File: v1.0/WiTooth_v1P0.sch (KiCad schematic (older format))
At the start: 51 parts, among them P1 USB_A, P2 JTAG, P3 CONN_01X04, P4 CONN_01X20, P5 CONN_01X20, Q1 Q_NPN_EBC, Q2 Q_NPN_EBC, SW1 RESET, SW2 Switch_SPDT_x2, SW3 USER_SW, U1 AMS1117-3V3, U2 CP2102, U3 ESP-32_WROOM32_Rectangle, Y1 Crystal

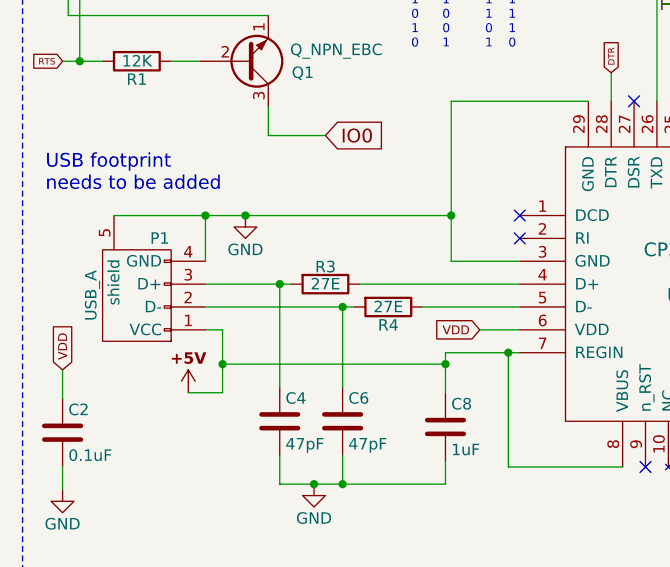
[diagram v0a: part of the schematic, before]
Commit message: schematic half verified; footprint association done
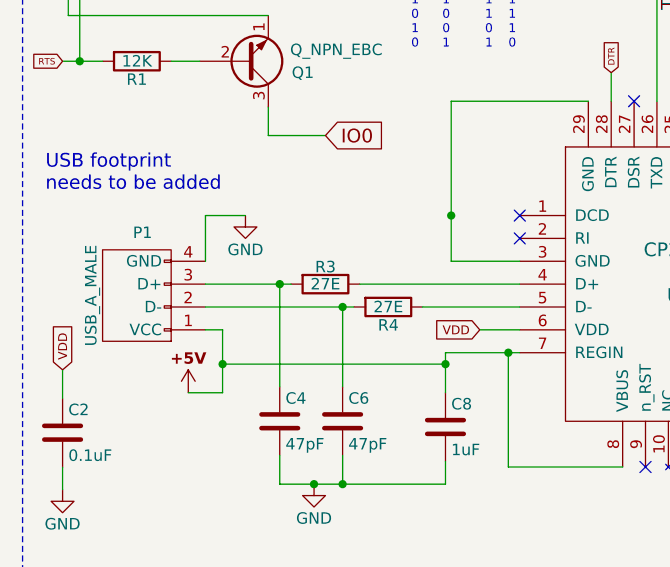
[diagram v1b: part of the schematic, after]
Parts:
- removed P1: USB_A, symbol USB_A
- added P1: USB_A_MALE, USB:usb-PCB_male, symbol USB_A_MALE
- U3: footprint (none) -> ESP-32:ESP32-WROOM
- Y1: footprint (none) -> Crystals:Crystal_AT310_d3.0mm_l10.0mm_Horizontal_1EP_style1
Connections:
- net +5V: now also P1.1 (VCC)
- net GND: now also P1.4 (GND); no longer U2.29 (GND), U2.3 (GND)
- net at C6.1, R4.2: now also P1.2 (D-)
- net at C4.1, R3.2: now also P1.3 (D+)
- new net: U2.29 (GND), U2.3 (GND)

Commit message: all changes done; schematic verified
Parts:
- removed C3: DNM, Capacitors_SMD:C_0805_HandSoldering, symbol C_Small
- removed C7: 22uF, Capacitors_SMD:C_0805_HandSoldering, symbol C
- removed R6: 5K, Resistors_SMD:R_0805_HandSoldering, symbol R
- C1: value 0.1uF -> 10uF
- C4: renamed from C5; value 47uF -> 10uF
- R11: renamed from R12; value 1K -> 470E
- R13: renamed from R14; value 10K -> 5K
- R7: renamed from R10; value 12K -> 470E
- renumbered C12 to C10, C13 to C11, C14 to C12, C15 to C13, C4 to C3, C6 to C5, C8 to C6, C9 to C7, C10 to C8, C11 to C9, R11 to R10, R13 to R12, R15 to R14, R16 to R15, R17 to R16, R5 to R4, R4 to R5, R7 to R6
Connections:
- net +3V3: now also R13.2; no longer R13.1
- net IO27: now also R7.2
- net IO32: no longer R7.2
- net at SW2.1 (A): now also R13.1; no longer R13.2
- net CTS: no longer names the net of U2.23 (CTS)
- no-connect marks 4 -> 5
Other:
- note removed: "check if switch\nis required\nor push button"
- moved on the sheet: C7, D1, D4, D5, R10, R11, R13, R4, R6, R7, SW2A

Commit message: initial placement started
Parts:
- U1: footprint TO_SOT_Packages_SMD:SOT-223-3Lead_TabPin2 -> TO_SOT_Packages_SMD:SOT-223
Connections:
- net GND: now also U3.39 (GND)
- no-connect marks 5 -> 7
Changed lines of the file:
@@
 F 0 "U1" H 1500 875 50  0000 C CNN
 F 1 "AMS1117-3V3" H 1400 1375 50  0000 C CNN
-F 2 "TO_SOT_Packages_SMD:SOT-223-3Lead_TabPin2" H 1400 1125 50  0001 C CNN
+F 2 "TO_SOT_Packages_SMD:SOT-223" H 1400 1125 50  0001 C CNN
 F 3 "" H 1500 875 50  0000 C CNN
 F 4 "LM1117 800-mA Low-Dropout Linear Regulator" H 1800 1175 61  0001 C CNN "DESC"
@@
 	1700 1125 2125 1125
 NoConn ~ 3600 3850
+NoConn ~ 3450 5450
+NoConn ~ 3550 5450
+Wire Wire Line
+	9075 3675 8825 3675
+Connection ~ 8825 3675
 $EndSCHEMATC

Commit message: basic placement done
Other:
- note removed: "Crystal footprint\nneeds to be added"
- note removed: "ESP32 footprint\nneeds to be added"
- note removed: "USB footprint\nneeds to be added"
- moved on the sheet: C2, P2, P3
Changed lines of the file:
@@
 L CONN_01X04 P3
 U 1 1 5898386C
-P 2925 6550
-F 0 "P3" H 2925 6800 50  0000 C CNN
-F 1 "CONN_01X04" V 3025 6550 50  0000 C CNN
-F 2 "Pin_Headers:Pin_Header_Straight_1x04_Pitch2.54mm" H 2925 6550 50  0001 C CNN
-F 3 "" H 2925 6550 50  0000 C CNN
-	1    2925 6550
+P 3550 6550
+F 0 "P3" H 3550 6800 50  0000 C CNN
+F 1 "CONN_01X04" V 3650 6550 50  0000 C CNN
+F 2 "Pin_Headers:Pin_Header_Straight_1x04_Pitch2.54mm" H 3550 6550 50  0001 C CNN
+F 3 "" H 3550 6550 50  0000 C CNN
+	1    3550 6550
 	-1   0    0    -1
 $EndComp
@@
 L +3V3 #PWR021
 U 1 1 58983CE6
-P 3350 6400
-F 0 "#PWR021" H 3350 6250 50  0001 C CNN
-F 1 "+3V3" H 3350 6550 50  0001 C CNN
-F 2 "" H 3350 6400 50  0000 C CNN
-F 3 "" H 3350 6400 50  0000 C CNN
-	1    3350 6400
+P 3975 6400
+F 0 "#PWR021" H 3975 6250 50  0001 C CNN
+F 1 "+3V3" H 3975 6550 50  0001 C CNN
+F 2 "" H 3975 6400 50  0000 C CNN
+F 3 "" H 3975 6400 50  0000 C CNN
+	1    3975 6400
 	1    0    0    -1
 $EndComp
@@
 L GND #PWR022
 U 1 1 58983F49
-P 3375 6700
-F 0 "#PWR022" H 3375 6450 50  0001 C CNN
-F 1 "GND" H 3375 6550 50  0000 C CNN
-F 2 "" H 3375 6700 50  0000 C CNN
-F 3 "" H 3375 6700 50  0000 C CNN
-	1    3375 6700
-	1    0    0    -1
-$EndComp
-Text GLabel 3350 6500 2    28   Input ~ 0
+P 4000 6700
+F 0 "#PWR022" H 4000 6450 50  0001 C CNN
+F 1 "GND" H 4000 6550 50  0000 C CNN
+F 2 "" H 4000 6700 50  0000 C CNN
+F 3 "" H 4000 6700 50  0000 C CNN
+	1    4000 6700
+	1    0    0    -1
+$EndComp
+Text GLabel 3975 6500 2    28   Input ~ 0
 TXD0
-Text GLabel 3350 6600 2    28   Input ~ 0
+Text GLabel 3975 6600 2    28   Input ~ 0
 RXD0
-Text Notes 2800 7050 0    39   ~ 0
+Text Notes 3425 7050 0    39   ~ 0
 Programming Connector\nfor WiTooth use only
 $Comp
@@
 Text Label 3400 3450 1    60   ~ 0
 TXD0
-Text GLabel 700  5025 1    39   Input ~ 0
+Text GLabel 825  6250 1    39   Input ~ 0
 VDD
 $Comp
 L C C2
 U 1 1 5899E045
-P 700 5300
-F 0 "C2" H 725 5400 50  0000 L CNN
-F 1 "0.1uF" H 725 5200 50  0000 L CNN
-F 2 "Capacitors_SMD:C_0805_HandSoldering" H 738 5150 50  0001 C CNN
-F 3 "" H 700 5300 50  0000 C CNN
-	1    700  5300
+P 825 6525
+F 0 "C2" H 850 6625 50  0000 L CNN
+F 1 "0.1uF" H 850 6425 50  0000 L CNN
+F 2 "Capacitors_SMD:C_0805_HandSoldering" H 863 6375 50  0001 C CNN
+F 3 "" H 825 6525 50  0000 C CNN
+	1    825  6525
 	1    0    0    -1
 $EndComp
@@
 L GND #PWR027
 U 1 1 5899E0E6
-P 700 5550
-F 0 "#PWR027" H 700 5300 50  0001 C CNN
-F 1 "GND" H 700 5400 50  0000 C CNN
-F 2 "" H 700 5550 50  0000 C CNN
-F 3 "" H 700 5550 50  0000 C CNN
-	1    700  5550
-	1    0    0    -1
-$EndComp
-Text Notes 2725 6100 0    60   ~ 0
+P 825 6775
+F 0 "#PWR027" H 825 6525 50  0001 C CNN
+F 1 "GND" H 825 6625 50  0000 C CNN
+F 2 "" H 825 6775 50  0000 C CNN
+F 3 "" H 825 6775 50  0000 C CNN
+	1    825  6775
+	1    0    0    -1
+$EndComp
+Text Notes 3350 6100 0    60   ~ 0
 External Programming
 Text Notes 1000 2700 0    60   ~ 0
@@
 L JTAG P2
 U 1 1 589A9CE9
-P 1500 6450
-F 0 "P2" H 1450 6350 60  0000 C CNN
-F 1 "JTAG" H 1250 6750 60  0000 C CNN
-F 2 "Pin_Headers:Pin_Header_Straight_2x05_Pitch1.27mm_SMD" H 1500 6450 60  0001 C CNN
-F 3 "" H 1500 6450 60  0001 C CNN
-	1    1500 6450
+P 2150 6500
+F 0 "P2" H 2100 6400 60  0000 C CNN
+F 1 "JTAG" H 1900 6800 60  0000 C CNN
+F 2 "Pin_Headers:Pin_Header_Straight_2x05_Pitch1.27mm_SMD" H 2150 6500 60  0001 C CNN
+F 3 "" H 2150 6500 60  0001 C CNN
+	1    2150 6500
 	1    0    0    -1
 $EndComp
@@
 L +3V3 #PWR029
 U 1 1 589AAAC8
-P 625 6300
-F 0 "#PWR029" H 625 6150 50  0001 C CNN
-F 1 "+3V3" H 625 6440 50  0001 C CNN
-F 2 "" H 625 6300 50  0000 C CNN
-F 3 "" H 625 6300 50  0000 C CNN
-	1    625  6300
+P 1275 6350
+F 0 "#PWR029" H 1275 6200 50  0001 C CNN
+F 1 "+3V3" H 1275 6490 50  0001 C CNN
+F 2 "" H 1275 6350 50  0000 C CNN
+F 3 "" H 1275 6350 50  0000 C CNN
+	1    1275 6350
 	1    0    0    -1
 $EndComp
@@
 L GND #PWR030
 U 1 1 589AAF5D
-P 625 6725
-F 0 "#PWR030" H 625 6475 50  0001 C CNN
-F 1 "GND" H 625 6575 50  0000 C CNN
-F 2 "" H 625 6725 50  0000 C CNN
-F 3 "" H 625 6725 50  0000 C CNN
-	1    625  6725
-	1    0    0    -1
-$EndComp
-Text GLabel 2325 6300 2    39   Input ~ 0
+P 1275 6775
+F 0 "#PWR030" H 1275 6525 50  0001 C CNN
+F 1 "GND" H 1275 6625 50  0000 C CNN
+F 2 "" H 1275 6775 50  0000 C CNN
+F 3 "" H 1275 6775 50  0000 C CNN
+	1    1275 6775
+	1    0    0    -1
+$EndComp
+Text GLabel 2975 6350 2    39   Input ~ 0
 IO14
-Text GLabel 2325 6400 2    39   Input ~ 0
+Text GLabel 2975 6450 2    39   Input ~ 0
 IO13
-Text GLabel 2325 6500 2    39   Input ~ 0
+Text GLabel 2975 6550 2    39   Input ~ 0
 IO15
-Text GLabel 2325 6600 2    39   Input ~ 0
+Text GLabel 2975 6650 2    39   Input ~ 0
 IO12
-Text GLabel 2325 6700 2    39   Input ~ 0
+Text GLabel 2975 6750 2    39   Input ~ 0
 EN
-Text Notes 1100 6025 0    59   ~ 0
+Text Notes 1750 6075 0    59   ~ 0
 JTAG programming
 $Comp
@@
 Text Notes 7525 2975 0    39   ~ 0
 2
-Text Notes 7125 4050 0    60   ~ 0
-Crystal footprint\nneeds to be added
-Text Notes 9525 4325 0    60   ~ 0
-ESP32 footprint\nneeds to be added
-Text Notes 625  4250 0    60   ~ 0
-USB footprint\nneeds to be added
 $Comp
 L USB_A_MALE P1
@@
 	4075 1700 4075 1825
 Wire Wire Line
-	3125 6400 3350 6400
-Wire Wire Line
-	3350 6500 3125 6500
-Wire Wire Line
-	3125 6600 3350 6600
-Wire Wire Line
-	3375 6700 3125 6700
+	3750 6400 3975 6400
+Wire Wire Line
+	3975 6500 3750 6500
+Wire Wire Line
+	3750 6600 3975 6600
+Wire Wire Line
+	4000 6700 3750 6700
 Wire Wire Line
 	700  1125 1100 1125
@@
 	3400 3850 3400 3225
 Wire Wire Line
-	700  5450 700  5550
-Wire Wire Line
-	700  5025 700  5150
+	825  6675 825  6775
+Wire Wire Line
+	825  6250 825  6375
 Wire Wire Line
 	700  3075 900  3075
@@
 	7975 3050 8050 3050
 Wire Wire Line
-	625  6300 800  6300
-Wire Wire Line
-	800  6700 625  6700
-Wire Wire Line
-	625  6400 625  6725
-Wire Wire Line
-	625  6500 800  6500
-Connection ~ 625  6700
-Wire Wire Line
-	625  6400 800  6400
-Connection ~ 625  6500
-Wire Wire Line
-	2150 6300 2325 6300
-Wire Wire Line
-	2325 6400 2150 6400
-Wire Wire Line
-	2150 6500 2325 6500
-Wire Wire Line
-	2325 6600 2150 6600
-Wire Wire Line
-	2150 6700 2325 6700
+	1275 6350 1450 6350
+Wire Wire Line
+	1450 6750 1275 6750
+Wire Wire Line
+	1275 6450 1275 6775
+Wire Wire Line
+	1275 6550 1450 6550
+Connection ~ 1275 6750
+Wire Wire Line
+	1275 6450 1450 6450
+Connection ~ 1275 6550
+Wire Wire Line
+	2800 6350 2975 6350
+Wire Wire Line
+	2975 6450 2800 6450
+Wire Wire Line
+	2800 6550 2975 6550
+Wire Wire Line
+	2975 6650 2800 6650
+Wire Wire Line
+	2800 6750 2975 6750
 Wire Notes Line
 	525  2325 4425 2325

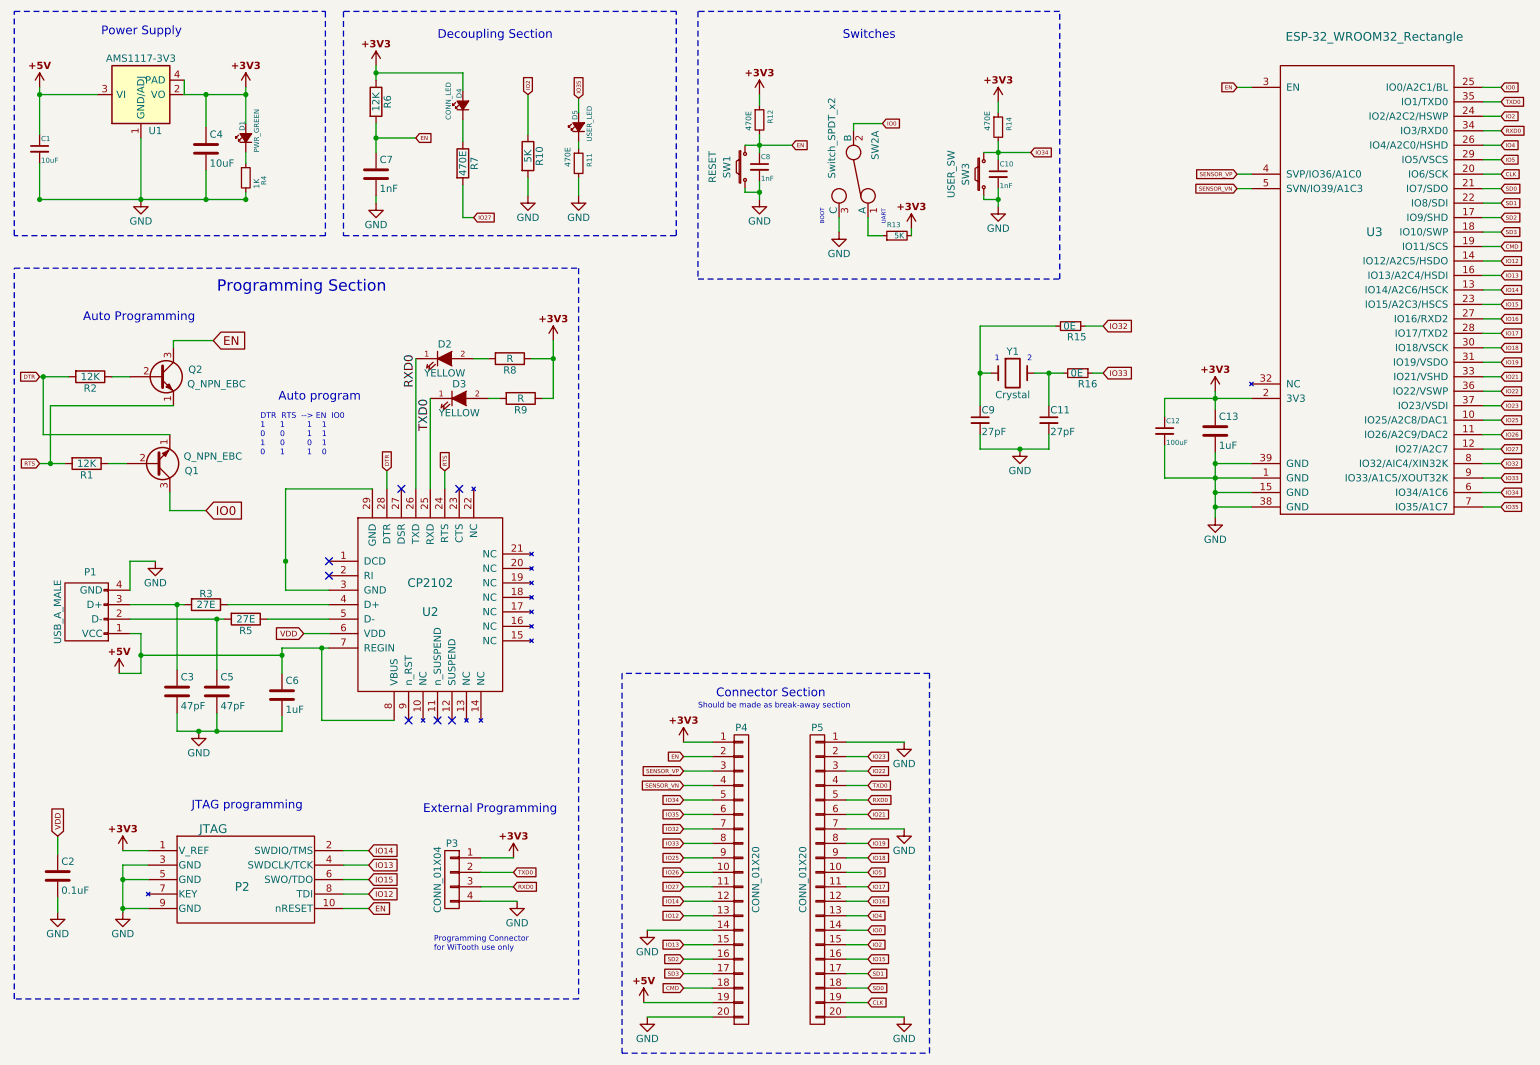
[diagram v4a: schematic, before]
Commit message: schematic updated and some parts removed; layout work started
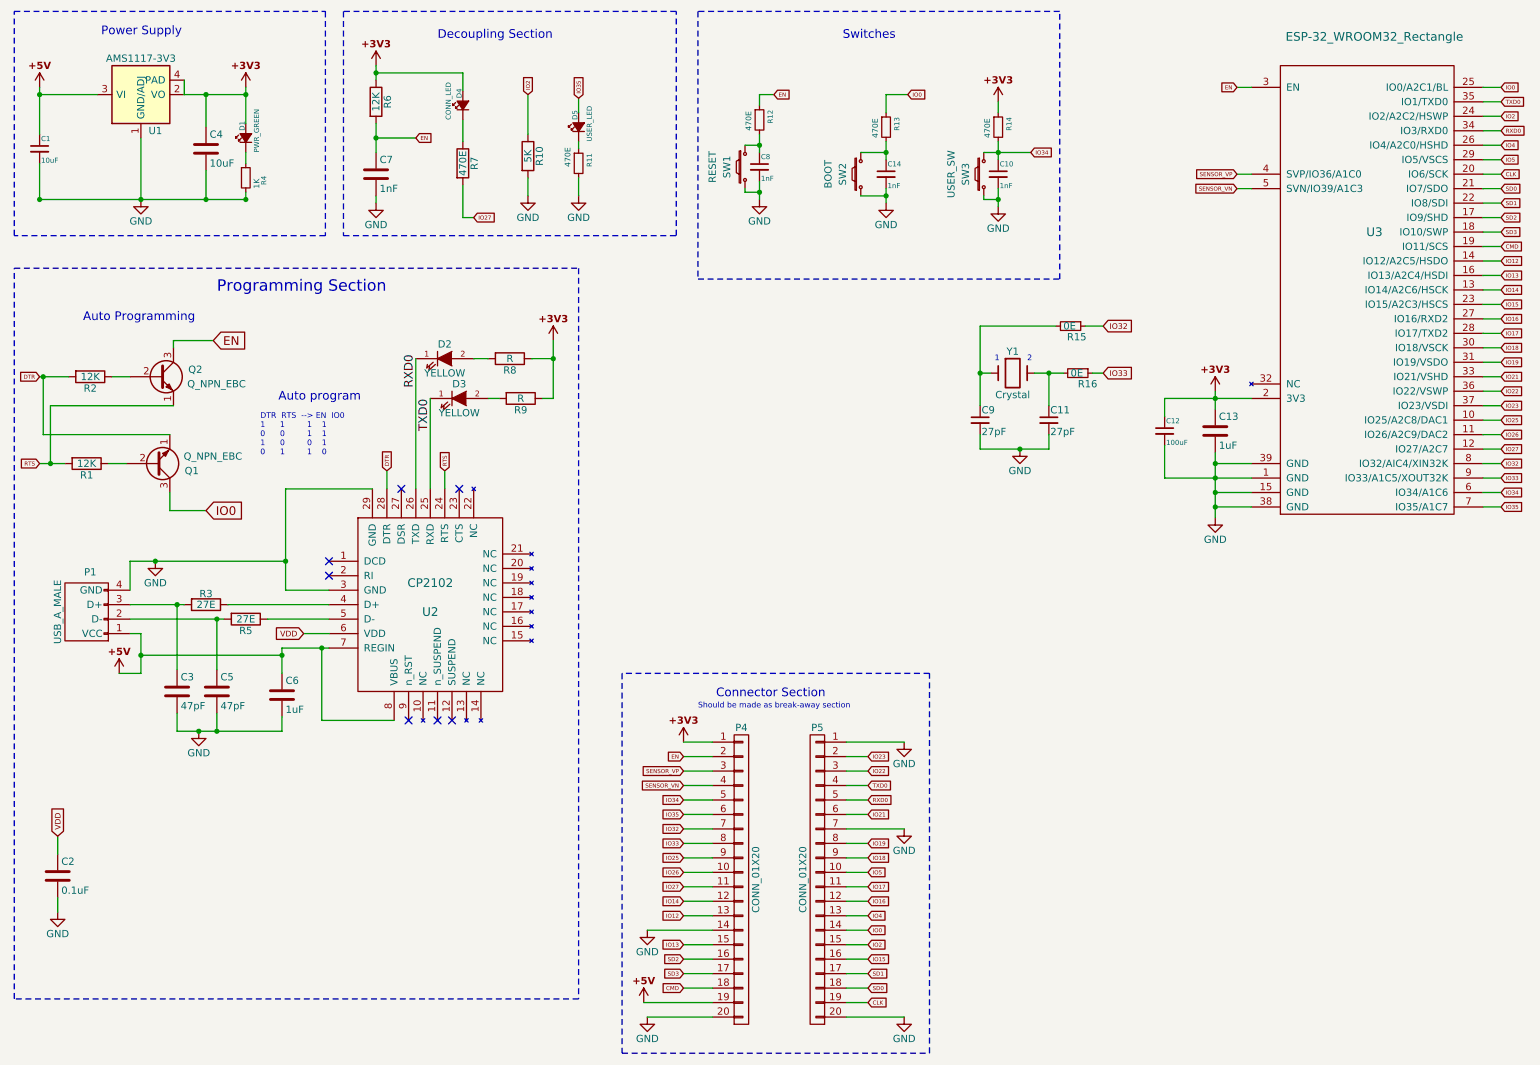
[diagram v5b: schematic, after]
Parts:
- removed P2: JTAG, Pin_Headers:Pin_Header_Straight_2x05_Pitch1.27mm_SMD, symbol JTAG
- removed P3: CONN_01X04, Pin_Headers:Pin_Header_Straight_1x04_Pitch2.54mm, symbol CONN_01X04
- removed SW2: Switch_SPDT_x2, Buttons_Switches_SMD:SW_SPDT_PCM12, symbol Switch_SPDT_x2
- added C14: 1nF, Capacitors_SMD:C_0805_HandSoldering, symbol C_Small
- added SW2: BOOT, switches:SW_SPST_B3U-1000P_SUNROM, symbol SW_PUSH_SMALL_H
- R13: value 5K -> 470E
- SW1, SW3: footprint switches:SW_SPST_B3U-1000P-B_SUNROM -> switches:SW_SPST_B3U-1000P_SUNROM
- U3: footprint ESP-32:ESP32-WROOM -> ESP-32:ESP32-WROOM_SMALLER_FOOTPRINT
- Y1: footprint Crystals:Crystal_AT310_d3.0mm_l10.0mm_Horizontal_1EP_style1 -> Crystals:Crystal_SMD_0603-2pin_6.0x3.5mm_HandSoldering
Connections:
- net +3V3: no longer R12.1, R13.2
- net EN: now also R12.1; no longer C8.1, R12.2, SW1.2
- net GND: now also U2.29 (GND), U2.3 (GND), C14.2, SW2.1
- net IO0: now also R13.1
- new net: C8.1, R12.2, SW1.2
- new net: C14.1, R13.2, SW2.2
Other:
- note removed: "BOOT"
- note removed: "External Programming"
- note removed: "JTAG programming"
- note removed: "Programming Connector\nfor WiTooth use only"
- note removed: "UART"
- moved on the sheet: R13
